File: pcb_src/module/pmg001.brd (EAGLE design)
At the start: 22.2 x 16.5 mm, 42 parts, among them IC1 APX803D-29SAG-7, IC2 ATTINY1616-MNR, IC3 LD56100DPU30R, IC4 IP2312, IC5 TMP102AIDRLR, IC6 DMP3013SFV-7, IC9 INA219AIDCNR, U1 ADS1015IDGSR

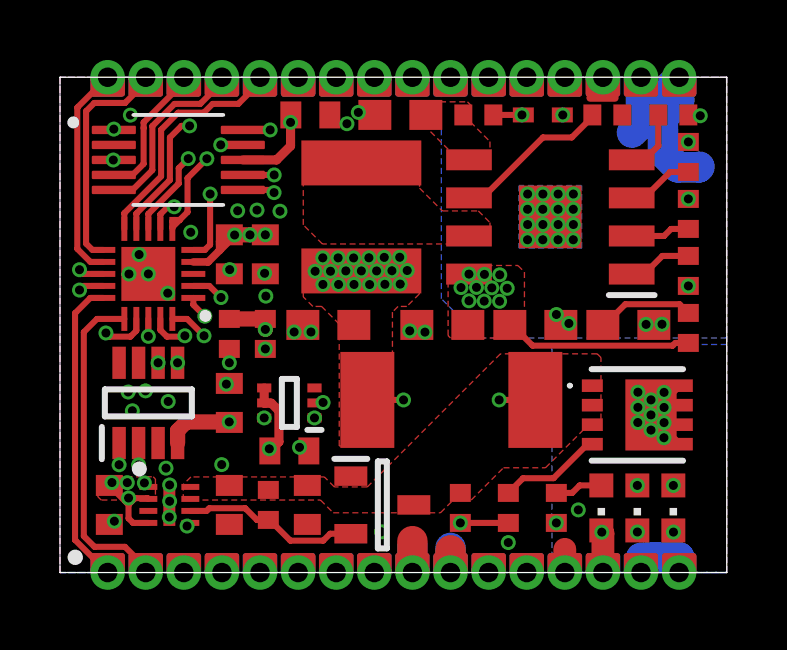
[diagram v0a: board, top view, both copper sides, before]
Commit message: Module and cover board revised. Datasheet revised. Code added.
Updated with one additional component, added cutout to cover board. Updated documentation accordingly.  Added default program.
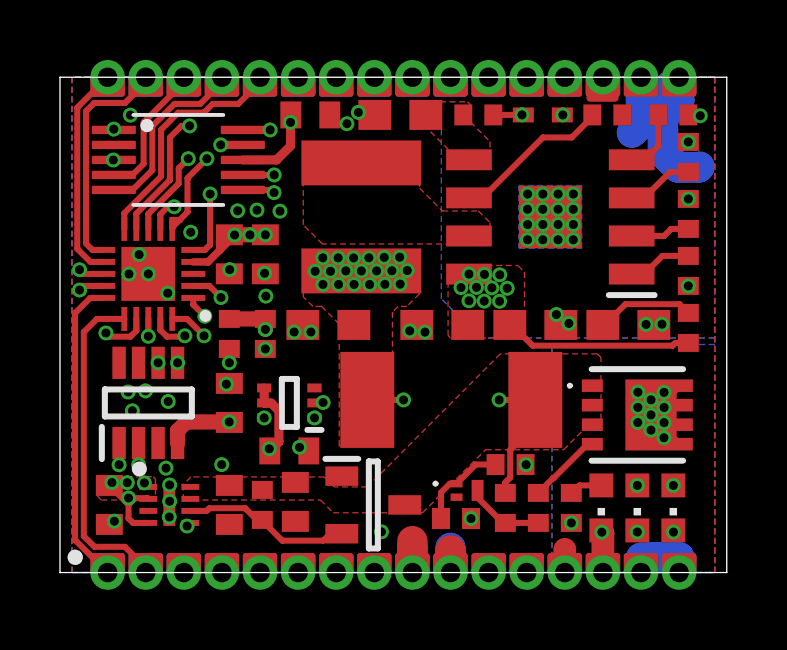
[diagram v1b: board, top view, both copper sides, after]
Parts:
- added Q1: PMZ290UNE2YL, edrtech_lib:PMZ290UNE2YL
- added R13: 20K, rcl:R0402
- added R9: 150R, rcl:R0402
- moved R14 1.50 mm to (14.8, 2.15)
- moved R16 1.00 mm to (15.9, 2.15)
- moved R8 0.50 mm to (17.0, 2.15)
- moved C1 0.41 mm to (7.84, 2.35)
- moved IC1 0.30 mm to (10.4, 2.25)
- moved R1 0.20 mm to (6.74, 2.25)
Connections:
- new net N$1: Q1.1, R13.2, R9.2
- new net P_ON_DS: Q1.3, R14.1, R16.1
- net GND: now also Q1.2, R13.1
- net P_ON: now also R9.1; no longer R14.1, R16.1
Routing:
- net BTAP: track 16.9 -> 20.4 mm
- net N$1: track 0.00 -> 3.07 mm
- net P_ON_DS: track 0.00 -> 2.61 mm
- net P_ON: track 21.7 -> 20.3 mm
- net N$6: track 3.47 -> 2.47 mm
- net N$2: track 1.60 -> 1.10 mm
- net GND: vias 62 -> 61
